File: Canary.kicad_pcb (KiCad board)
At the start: 4 copper layers, 56 x 38 mm, 85 parts, among them J1 CONN_ARM_CM_JTAG_SWD_10, J2 BMD-300-A-R, J3 20021311-00010T4LF, J4 USB4125-GF-A, J5 S2B-PH-SM4-TB, Q1 PMN30UNX, Q2 PMN42XPEAH, Q3 PMN30UNX, SW1 TL3301SPF160QJ, U1 DNP, U10 MCP73831T-2ATI_OT, U11 MIC2288YD5, U2 SHTC3, U3 SGP40, U4 MAX6071BAUT21T, U5 LMP91000, U6 SPEC-110-902, U7 MCP6041T-I_OT, U8 RT6150AGQW, U9 LP5907MFX-3.2, Y1 32.7680 kHz

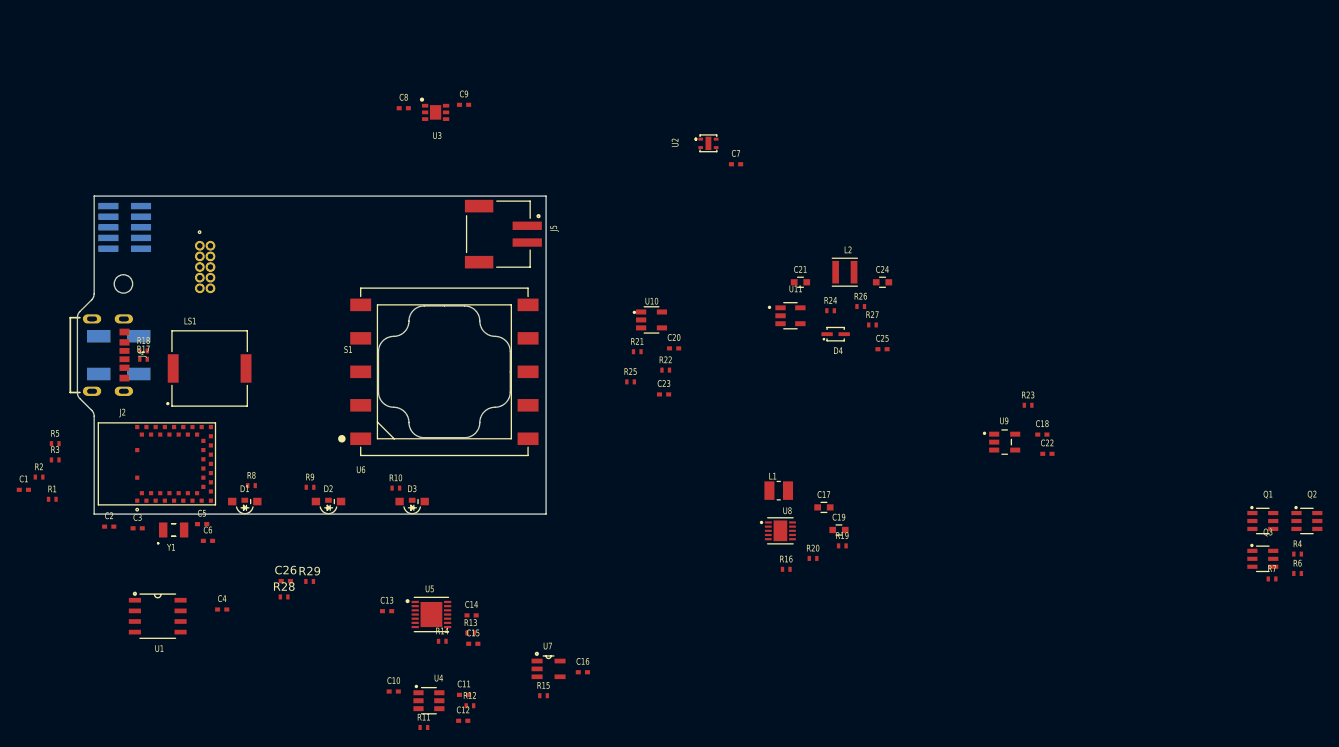
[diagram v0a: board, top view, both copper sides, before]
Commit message: Group components
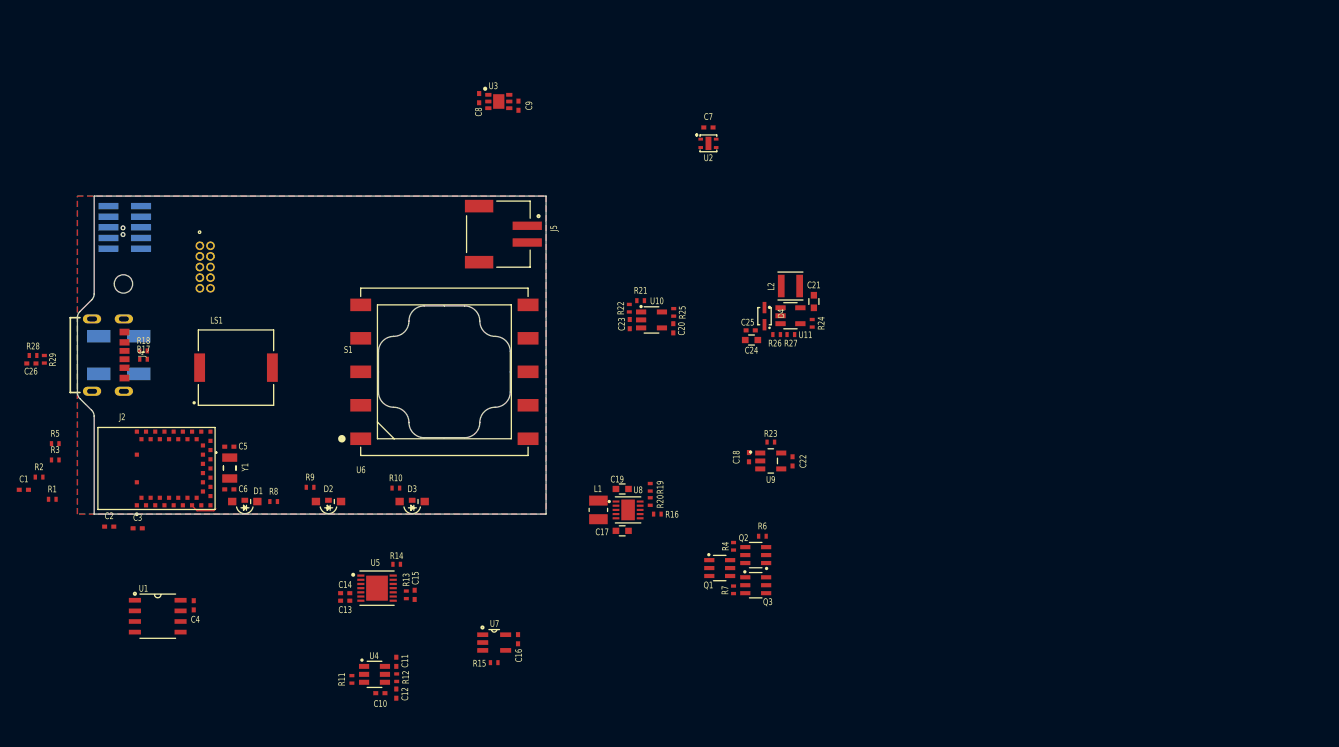
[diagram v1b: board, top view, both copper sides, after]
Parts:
- J3: value 20021311-00010T4LF -> CONN_20021311-00010T4LF_AMP
- moved R4 67.4 mm to (119.4, 89.8), turned to 270 degrees
- moved Q2 66.0 mm to (122.0, 90.9), turned to 180 degrees
- moved Q1 65.1 mm to (117.7, 92.5)
- moved R7 64.4 mm to (119.4, 95.0), turned to 270 degrees
- moved R6 64.1 mm to (122.8, 88.7)
- moved Q3 60.7 mm to (122.0, 94.5)
- moved R28 41.6 mm to (35.7, 67.0), turned to 180 degrees
- moved R29 41.3 mm to (37.0, 67.5), turned to 270 degrees
- moved C26 40.0 mm to (35.5, 68.0), turned to 180 degrees
- moved C18 35.2 mm to (121.2, 79.2), turned to 270 degrees
- moved R23 31.1 mm to (123.8, 77.4), turned to 180 degrees
- moved C22 30.5 mm to (126.5, 79.7), turned to 270 degrees
- moved U9 28.0 mm to (123.8, 79.7)
- moved C19 26.4 mm to (106.1, 83.0)
- moved C17 24.3 mm to (106.1, 88.0)
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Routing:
- net /XTAL1: track 0.05 -> 3.25 mm
- net GND: vias 0 -> 2
- added copper zone on B.Cu, net GND
- added copper zone on F.Cu, net GND
- added copper zone on GND.Cu, net GND
- added copper zone on PWR.Cu, net VDD

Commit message: Reannotate, fix BMD reference
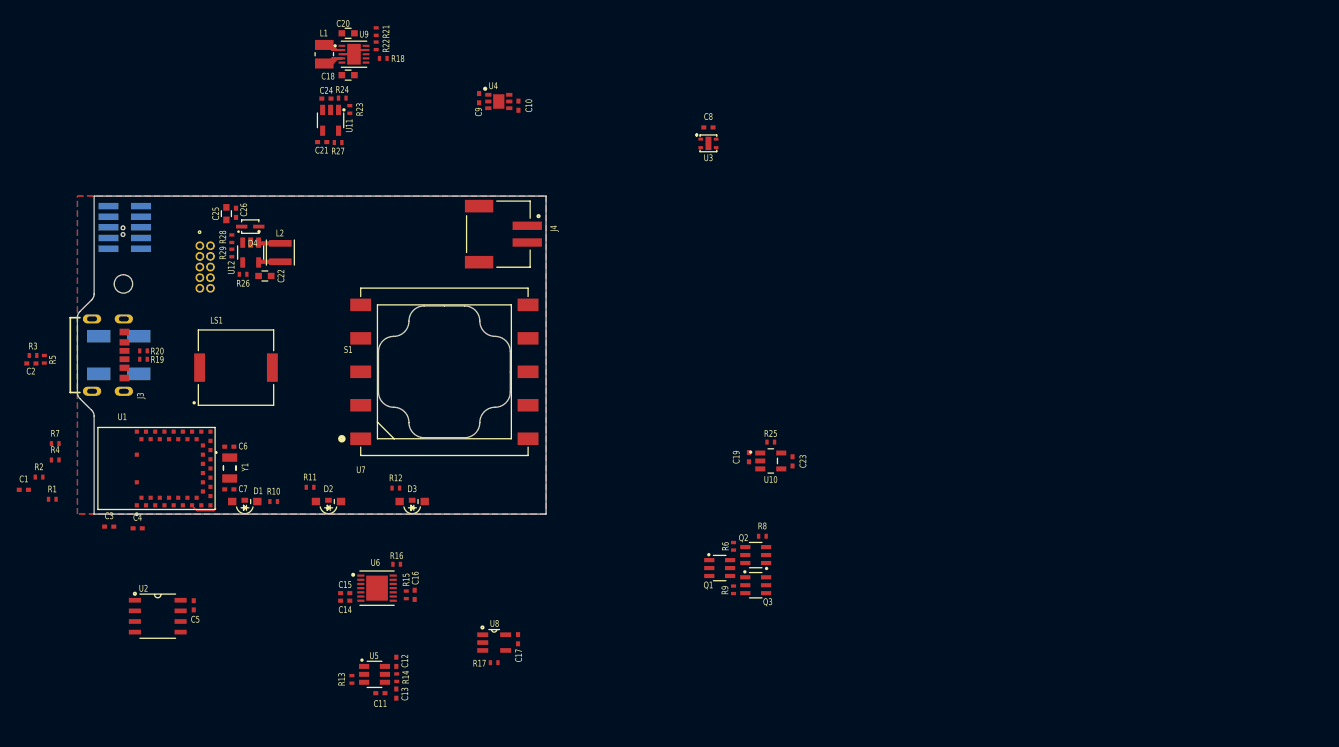
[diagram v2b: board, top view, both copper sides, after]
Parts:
- removed the C17 at (106.1, 88.0)
- removed the C19 at (106.1, 83.0)
- removed the J2 at (50.5, 80.5)
- removed the R16 at (110.3, 86.0)
- removed the R19 at (109.5, 82.8)
- removed the R20 at (109.5, 84.5)
- removed the U8 at (106.8, 85.5)
- added C18: 10u, JetkovKiCADLib:C_0603, F.Cu at (73.3, 33.5)
- added C20: 10u, JetkovKiCADLib:C_0603, F.Cu at (73.3, 28.6)
- added R18: 1M, JetkovKiCADLib:R_0402_NoSilk, F.Cu at (77.5, 31.6)
- added R21: 487k, JetkovKiCADLib:R_0402_NoSilk, F.Cu at (76.7, 28.4)
- added R22: 86.6k, JetkovKiCADLib:R_0402_NoSilk, F.Cu at (76.7, 30.1)
- added U1: BMD-300-A-R, JetkovKiCADLib:BMD-300-A-R, F.Cu at (50.5, 80.5)
- added U9: RT6150AGQW, JetkovKiCADLib:RT6150AGQW, F.Cu at (74.0, 31.1)
- J2: renamed from J3; value CONN_20021311-00010T4LF_AMP -> 20021311-00010T4LF
- moved R26 68.3 mm to (60.8, 57.4), turned to 180 degrees
- moved R29 67.5 mm to (59.5, 54.8), turned to 270 degrees
- moved R28 66.1 mm to (59.5, 53.1), turned to 270 degrees
- moved C22 65.7 mm to (63.4, 57.5), turned to 0 degrees
- moved U12 64.9 mm to (61.7, 54.8), turned to 270 degrees
- moved C25 64.5 mm to (58.8, 50.1), turned to 90 degrees
- moved L1 63.5 mm to (70.5, 31.1)
- moved C26 63.1 mm to (60.0, 50.0), turned to 90 degrees
- moved D4 62.4 mm to (61.6, 51.6), turned to 0 degrees
- moved L2 61.1 mm to (65.2, 54.8), turned to 90 degrees
- moved C21 47.5 mm to (70.2, 41.5), turned to 180 degrees
- moved C24 45.2 mm to (70.8, 36.4), turned to 0 degrees
- moved U11 45.2 mm to (71.2, 39.0), turned to 270 degrees
- moved R27 44.9 mm to (72.2, 41.6), turned to 0 degrees
- moved R24 42.5 mm to (72.7, 36.3), turned to 180 degrees
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- renumbered C9 to C10, C10 to C11, C11 to C12, C12 to C13, C13 to C14, C14 to C15, C15 to C16, C16 to C17, C18 to C19, C26 to C2, C20 to C21, C21 to C22, C22 to C23, C23 to C24, C24 to C25, C25 to C26, C2 to C3, C3 to C4, C4 to C5, C5 to C6, C6 to C7, C7 to C8, C8 to C9, J4 to J3, J5 to J4, R8 to R10, R9 to R11, R10 to R12, R11 to R13, R12 to R14, R13 to R15, R14 to R16, R15 to R17, R17 to R19, R18 to R20, R21 to R23, R22 to R24, R23 to R25, R24 to R26, R25 to R27, R26 to R28, R27 to R29, R28 to R3, R3 to R4, R29 to R5, R4 to R6, R5 to R7, R6 to R8, R7 to R9, U9 to U10, U10 to U11, U11 to U12, U1 to U2, U2 to U3, U3 to U4, U4 to U5, U5 to U6, U6 to U7, U7 to U8
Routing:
- net /Power/LVR_LX1: track 0.00 -> 5.42 mm
- net /Power/LVR_LX2: track 0.00 -> 5.00 mm
- net GND: track 0.00 -> 3.10 mm
- net /Power/HVR_SW: track 0.00 -> 2.64 mm
- net +BATT: track 0.00 -> 2.64 mm

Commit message: layout wip
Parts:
- moved Q1 80.6 mm to (47.4, 53.1)
- moved R9 80.5 mm to (49.1, 55.8)
- moved R6 80.1 mm to (49.4, 50.8), turned to 180 degrees
- moved Q2 79.8 mm to (51.8, 53.1)
- moved Q3 79.8 mm to (51.8, 56.7)
- moved R8 79.8 mm to (52.5, 50.8)
- moved C23 64.3 mm to (63.8, 65.2), turned to 180 degrees
- moved U10 62.8 mm to (63.4, 62.5), turned to 270 degrees
- moved C19 60.5 mm to (63.9, 60.0), turned to 180 degrees
- moved R25 60.1 mm to (65.7, 62.5), turned to 90 degrees
- moved C8 51.9 mm to (87.7, 83.0), turned to 180 degrees
- moved U3 48.3 mm to (88.0, 81.2), turned to 90 degrees
- moved C9 45.6 mm to (85.3, 81.7), turned to 90 degrees
- moved C10 45.4 mm to (80.6, 80.7), turned to 90 degrees
- moved U4 45.3 mm to (83.0, 81.2), turned to 180 degrees
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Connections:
- U4 pad 7: (no net) -> GND
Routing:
- net GND: track 3.10 -> 57.9 mm, vias 2 -> 50
- net VBUS: track 0.00 -> 51.8 mm
- net /PDRIVE_O: track 0.00 -> 17.7 mm
- net VDD: track 0.00 -> 7.34 mm, vias 0 -> 8
- net /XTAL1: track 3.25 -> 8.82 mm
- net VREF: track 0.00 -> 4.65 mm
- net /Power/HVR_SW: track 2.64 -> 7.00 mm
- net LMP_VOUT: track 0.00 -> 4.11 mm
- net +BATT: track 2.64 -> 5.14 mm
- net /Power/LVR_FB: track 0.00 -> 2.19 mm
- net /Power/HVR_FB: track 0.00 -> 2.18 mm
- net LMP_VOUT_B: track 0.00 -> 2.11 mm
- net /Power/USB_CC2: track 0.00 -> 1.82 mm
- net /Power/USB_CC1: track 0.00 -> 1.82 mm
- net /XTAL2: track 0.00 -> 1.78 mm
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- added copper zone on F.Cu, net +3V3
- added copper zone on PWR.Cu, net +3V3
- added copper zone on F.Cu, net +5V
- added copper zone on F.Cu, net +BATT
- added copper zone on F.Cu, net /Power/HVR_SW
- added copper zone on F.Cu, net VDD

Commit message: routing wip
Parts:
- moved C3 0.75 mm to (58.2, 81.5)
- moved C4 0.75 mm to (59.1, 81.5)
- moved R10 0.15 mm to (64.2, 84.5)
- moved R11 0.10 mm to (74.2, 84.5)
- moved R12 0.10 mm to (84.2, 84.5)
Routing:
- net LED_RED: track 0.00 -> 29.1 mm, vias 0 -> 2
- net LED_AMBER: track 0.00 -> 16.3 mm, vias 0 -> 2
- net LED_GREEN: track 0.00 -> 10.6 mm, vias 0 -> 2
- net /XTAL2: track 1.78 -> 11.2 mm
- net GND: track 57.9 -> 64.9 mm, vias 50 -> 55
- net +3V3: track 0.00 -> 4.72 mm, vias 10 -> 12
- net LMP_VOUT_B: track 2.11 -> 5.49 mm, vias 0 -> 1
- net Net-(D1-Pad1): track 0.00 -> 1.41 mm
- net Net-(D3-Pad1): track 0.00 -> 1.34 mm
- net Net-(D2-Pad1): track 0.00 -> 1.34 mm
- net /BAT_DIV: track 0.00 -> 0.80 mm, vias 0 -> 1

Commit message: Routing wip
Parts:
- moved C11 0.60 mm to (67.9, 66.2)
- moved C12 0.60 mm to (71.7, 68.1)
- moved R13 0.60 mm to (69.7, 62.8)
- moved R14 0.60 mm to (69.8, 68.1)
- moved U5 0.60 mm to (70.2, 65.5)
- moved C13 0.60 mm to (67.8, 68.1)
- moved C2 0.58 mm to (50.0, 60.8)
- moved R3 0.58 mm to (49.0, 61.0)
- moved R5 0.58 mm to (49.5, 62.3)
- moved C10 0.25 mm to (80.6, 80.5)
- moved C16 0.25 mm to (72.3, 74.0)
- moved C8 0.25 mm to (87.7, 82.8)
- moved C9 0.25 mm to (85.3, 81.5)
- moved R15 0.25 mm to (71.3, 74.0)
- moved U3 0.25 mm to (88.0, 80.9)
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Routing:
- net GND: track 64.9 -> 95.1 mm, vias 55 -> 65
- net /Potentiostat/SPEC_CE: track 0.00 -> 30.1 mm, vias 0 -> 2
- net SWO: track 0.00 -> 29.9 mm, vias 0 -> 1
- net ~RESET~: track 0.00 -> 29.2 mm, vias 0 -> 1
- net SWDCLK: track 0.00 -> 28.6 mm, vias 0 -> 1
- net /Potentiostat/SPEC_WE: track 0.00 -> 28.0 mm
- net SWDIO: track 0.00 -> 24.9 mm, vias 0 -> 1
- net PIEZO_PWM: track 0.00 -> 22.1 mm
- net /PDRIVE: track 0.00 -> 14.6 mm
- net /Potentiostat/SPEC_RE: track 0.00 -> 14.4 mm
- net VREF: track 4.65 -> 13.5 mm, vias 0 -> 3
- net /RBTN: track 0.00 -> 8.47 mm, vias 0 -> 1
- net +3V3: track 4.72 -> 12.0 mm, vias 12 -> 14
- net SPI_CLK: track 0.00 -> 4.97 mm, vias 0 -> 1
- net VDD: track 7.34 -> 10.9 mm, vias 8 -> 10
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- added copper zone on PWR.Cu, net +5V

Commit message: Routing wip
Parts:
- moved R4 33.2 mm to (71.5, 81.8), turned to 90 degrees
- moved R7 32.5 mm to (70.5, 81.8), turned to 90 degrees
- moved C9 1.05 mm to (84.2, 81.5)
- moved C10 1.05 mm to (79.5, 80.5)
- moved U4 1.05 mm to (81.9, 81.0)
- moved U3 0.05 mm to (88.0, 80.8)
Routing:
- net 3V3_PS: track 2.04 -> 42.5 mm, vias 1 -> 2
- net CHG_STAT: track 1.83 -> 29.1 mm
- net ~PM_RST~: track 0.00 -> 21.5 mm, vias 1 -> 2
- net VDD_EN: track 2.29 -> 23.2 mm, vias 1 -> 2
- net BUTTON: track 1.00 -> 16.9 mm, vias 0 -> 2
- net GND: track 95.1 -> 109.4 mm, vias 65 -> 67
- net VREF_EN: track 1.43 -> 15.6 mm
- net +BATT: track 5.14 -> 19.2 mm
- net LMP_VOUT_B: track 5.49 -> 19.0 mm, vias 1 -> 0
- net 5V_EN: track 1.31 -> 13.0 mm, vias 1 -> 0
- net ~FLASH_CS~: track 0.00 -> 10.8 mm
- net SPI_MISO: track 0.00 -> 8.91 mm, vias 1 -> 0
- net PM_UART_RXD: track 0.00 -> 8.57 mm
- net ~PM_SLEEP~: track 0.00 -> 7.03 mm
- net PM_UART_TXD: track 0.00 -> 6.40 mm
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
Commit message: Info tweaks
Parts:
- R12: value 500R -> 499R
- R13, R18, R26: value 1M -> 2M
- R3, R5, R6: value 100k -> 180k
- R8, R9: value 100R -> 470R
- S1: value SM-UART-04L -> DNP
- U7: value SPEC-110-902 -> DNP
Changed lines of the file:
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@@
     (add_net "Net-(D2-Pad1)")
     (add_net "Net-(D3-Pad1)")
+    (add_net "Net-(J1-Pad7)")
+    (add_net "Net-(J1-Pad8)")
+    (add_net "Net-(J1-Pad9)")
+    (add_net "Net-(J2-Pad6)")
+    (add_net "Net-(J2-Pad8)")
+    (add_net "Net-(U1-Pad10)")
+    (add_net "Net-(U1-Pad11)")
+    (add_net "Net-(U1-Pad15)")
+    (add_net "Net-(U1-Pad19)")
+    (add_net "Net-(U1-Pad9)")
+    (add_net "Net-(U2-Pad3)")
+    (add_net "Net-(U2-Pad7)")
     (add_net PIEZO_PWM)
     (add_net PM_UART_RXD)
@@
       (effects (font (size 0.8 0.6) (thickness 0.15)))
     )
-    (fp_text value SPEC-110-902 (at -0.15 -0.07) (layer F.Fab) hide
+    (fp_text value DNP (at -0.15 -0.07) (layer F.Fab) hide
       (effects (font (size 1 1) (thickness 0.15)))
     )
@@
       (effects (font (size 0.8 0.6) (thickness 0.15)))
     )
-    (fp_text value 100k (at 0 1.25) (layer F.Fab) hide
+    (fp_text value 180k (at 0 1.25) (layer F.Fab) hide
       (effects (font (size 1 1) (thickness 0.15)))
     )
@@
       (effects (font (size 0.8 0.6) (thickness 0.15)))
     )
-    (fp_text value 100k (at 0 1.25 90) (layer F.Fab) hide
+    (fp_text value 180k (at 0 1.25 90) (layer F.Fab) hide
       (effects (font (size 1 1) (thickness 0.15)))
     )
@@
       (effects (font (size 0.8 0.6) (thickness 0.15)))
     )
-    (fp_text value 100k (at 0 1.25) (layer F.Fab) hide
+    (fp_text value 180k (at 0 1.25) (layer F.Fab) hide
       (effects (font (size 1 1) (thickness 0.15)))
     )
@@
       (effects (font (size 0.8 0.6) (thickness 0.15)))
     )
-    (fp_text value 100R (at 0 1.25) (layer F.Fab) hide
+    (fp_text value 470R (at 0 1.25) (layer F.Fab) hide
       (effects (font (size 1 1) (thickness 0.15)))
     )
@@
       (effects (font (size 0.8 0.6) (thickness 0.15)))
     )
-    (fp_text value 100R (at 0 1.25 90) (layer F.Fab) hide
+    (fp_text value 470R (at 0 1.25 90) (layer F.Fab) hide
       (effects (font (size 1 1) (thickness 0.15)))
     )
@@
       (effects (font (size 0.8 0.6) (thickness 0.15)))
     )
-    (fp_text value 500R (at 0 1.25) (layer F.Fab) hide
+    (fp_text value 499R (at 0 1.25) (layer F.Fab) hide
       (effects (font (size 1 1) (thickness 0.15)))
     )
@@
       (effects (font (size 0.8 0.6) (thickness 0.15)))
     )
-    (fp_text value 1M (at 0 1.25) (layer F.Fab) hide
+    (fp_text value 2M (at 0 1.25) (layer F.Fab) hide
       (effects (font (size 1 1) (thickness 0.15)))
     )
@@
       (effects (font (size 0.8 0.6) (thickness 0.15)))
     )
-    (fp_text value 1M (at 0 1.25 90) (layer F.Fab) hide
+    (fp_text value 2M (at 0 1.25 90) (layer F.Fab) hide
       (effects (font (size 1 1) (thickness 0.15)))
     )
@@
       (effects (font (size 0.8 0.6) (thickness 0.15)))
     )
-    (fp_text value 1M (at 0 1.25 90) (layer F.Fab) hide
+    (fp_text value 2M (at 0 1.25 90) (layer F.Fab) hide
       (effects (font (size 1 1) (thickness 0.15)))
     )
@@
       (effects (font (size 0.8 0.6) (thickness 0.15)))
     )
-    (fp_text value SM-UART-04L (at 23.1 16.9) (layer F.Fab) hide
+    (fp_text value DNP (at 23.1 16.9) (layer F.Fab) hide
       (effects (font (size 1 1) (thickness 0.15)))
     )

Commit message: Routing done (needs review)
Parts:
- moved R7 2.59 mm to (72.9, 80.8), turned to 270 degrees
- moved C1 2.55 mm to (61.1, 73.6)
- moved R4 1.10 mm to (72.0, 80.8), turned to 270 degrees
- moved R2 0.84 mm to (60.2, 73.6)
- moved R1 0.84 mm to (60.2, 71.9)
- moved S1 0.42 mm to (50.3, 48.0)
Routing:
- net I2C_SDA: track 0.00 -> 51.9 mm, vias 1 -> 4
- net I2C_SCL: track 0.00 -> 49.2 mm, vias 0 -> 5
- net 5V_EN: track 13.0 -> 33.1 mm, vias 0 -> 2
- net ~LMP_EN~: track 4.47 -> 22.9 mm, vias 0 -> 2
- net PM_UART_RXD: track 8.57 -> 25.8 mm, vias 0 -> 1
- net PM_UART_TXD: track 6.40 -> 23.1 mm
- net VREF_EN: track 15.6 -> 31.4 mm, vias 0 -> 2
- net ~PM_SLEEP~: track 7.03 -> 21.5 mm
- net VDD: track 10.9 -> 23.3 mm, vias 10 -> 16
- net /BAT_DIV: track 6.12 -> 15.7 mm, vias 1 -> 2
- net PIEZO_PWM: track 27.4 -> 35.7 mm, vias 1 -> 2
- net GND: track 109.4 -> 117.4 mm, vias 67 -> 69
- net ~PM_RST~: track 21.5 -> 24.4 mm
- net +BATT: track 19.2 -> 21.4 mm
